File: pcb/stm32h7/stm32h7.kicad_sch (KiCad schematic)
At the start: 36 parts, among them SW2 SW_Push, SW3 SW_Push, U1 STM32H743VGTx, U11 TPS61169DCKR, U9 MT25QUxxxxxx1xW7, Y1 25MHz

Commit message: routing done
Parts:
- removed SW3: SW_Push, custom_comps:SW4_PTS815 SJM 250 SMTR LFS_CNK, symbol Switch:SW_Push
- added J6: Test Pads, custom_comps:2 Wire Pads, symbol Connector:Conn_01x02_Pin
- added SW1: SW_Push, custom_comps:vert_button_6mm, symbol Switch:SW_Push
- added SW3: SW_Push, SW4_PTS815 SJM 250 SMTR LFS_CNK, symbol PTS815_SJM_250_SMTR_LFS:PTS815_SJM_250_SMTR_LFS
- C14, C22: footprint (none) -> Capacitor_SMD:C_0402_1005Metric
- R2: footprint (none) -> Resistor_SMD:R_0402_1005Metric
- SW2: footprint custom_comps:SW4_PTS815 SJM 250 SMTR LFS_CNK -> SW4_PTS815 SJM 250 SMTR LFS_CNK; symbol Switch:SW_Push -> PTS815_SJM_250_SMTR_LFS:PTS815_SJM_250_SMTR_LFS
- U11: footprint DCK0005A_N -> custom_comps:DCK0005A_N
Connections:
- net +3V3: now also SW3.1, SW3.2
- net GND: now also SW2.3, SW2.4, Y1.2, SW1.2; no longer SW2.1, U1.24 (PA2), U1.32 (PC4), U1.33 (PC5), Y1.1
- net NRST: now also SW2.1
- net PH0: now also Y1.1; no longer Y1.2
- net at R1.1, U1.94 (BOOT0): now also SW3.3, SW3.4
- new net: J6.1 (Pin_1), U1.32 (PC4)
- new net: J6.2 (Pin_2), U1.24 (PA2)
- new net BTN: SW1.1, U1.33 (PC5)
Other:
- moved on the sheet: C5, C6, R1

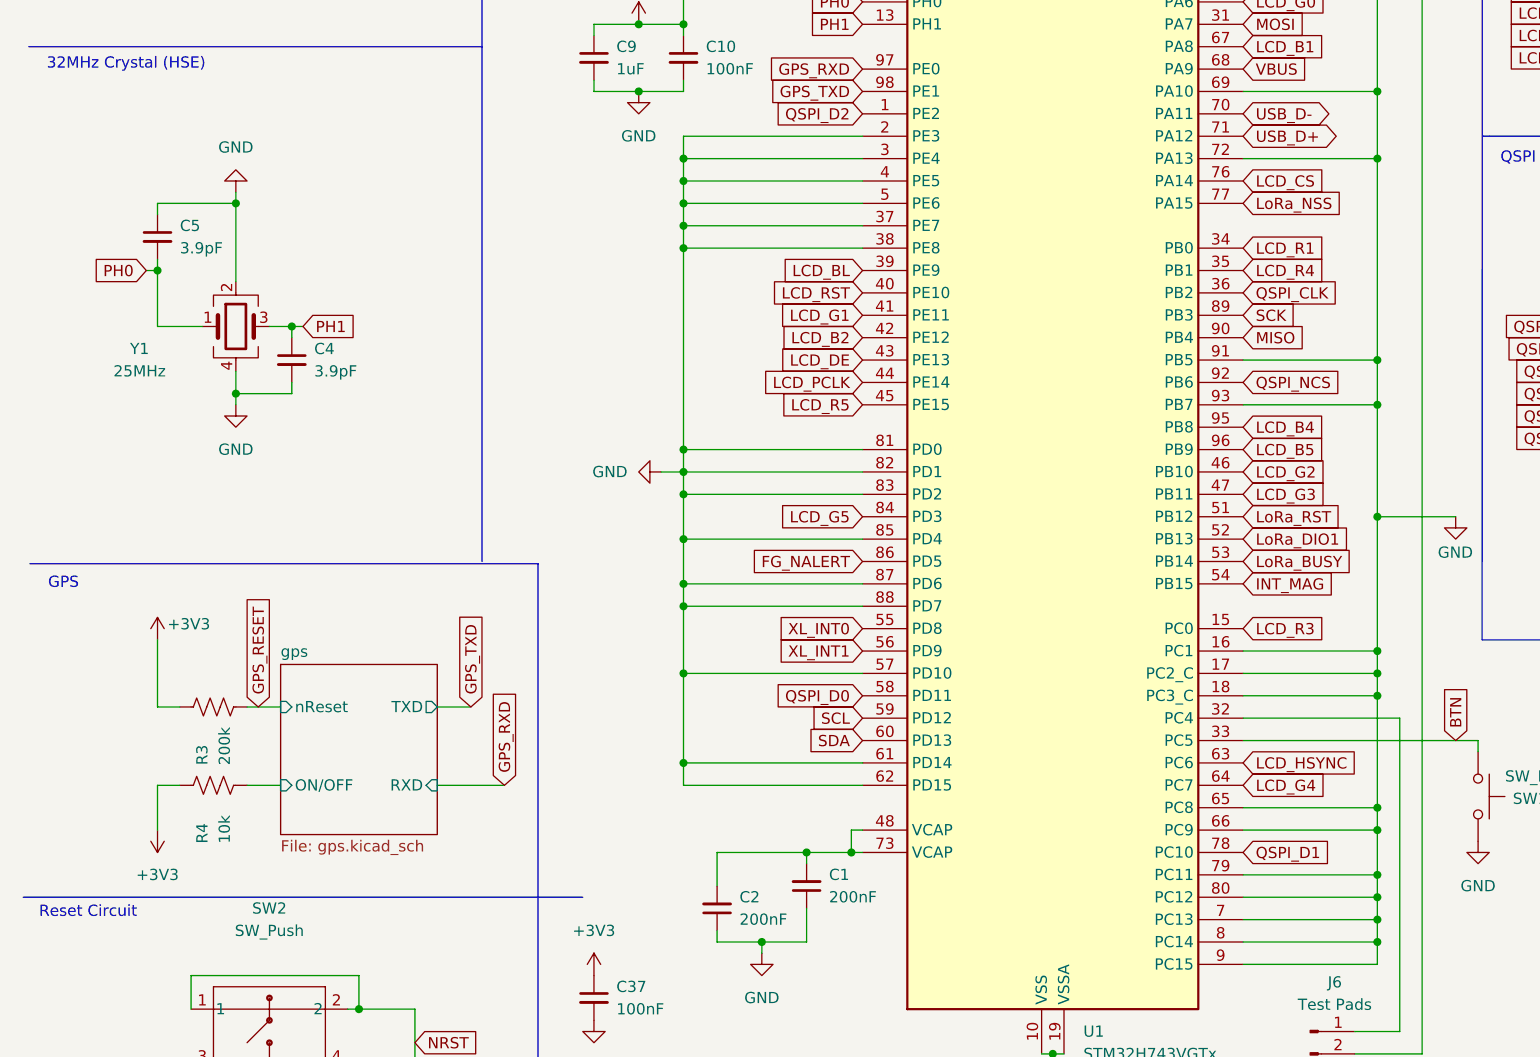
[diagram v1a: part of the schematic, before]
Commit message: fixed some footprints and added power switching mosfet for gps
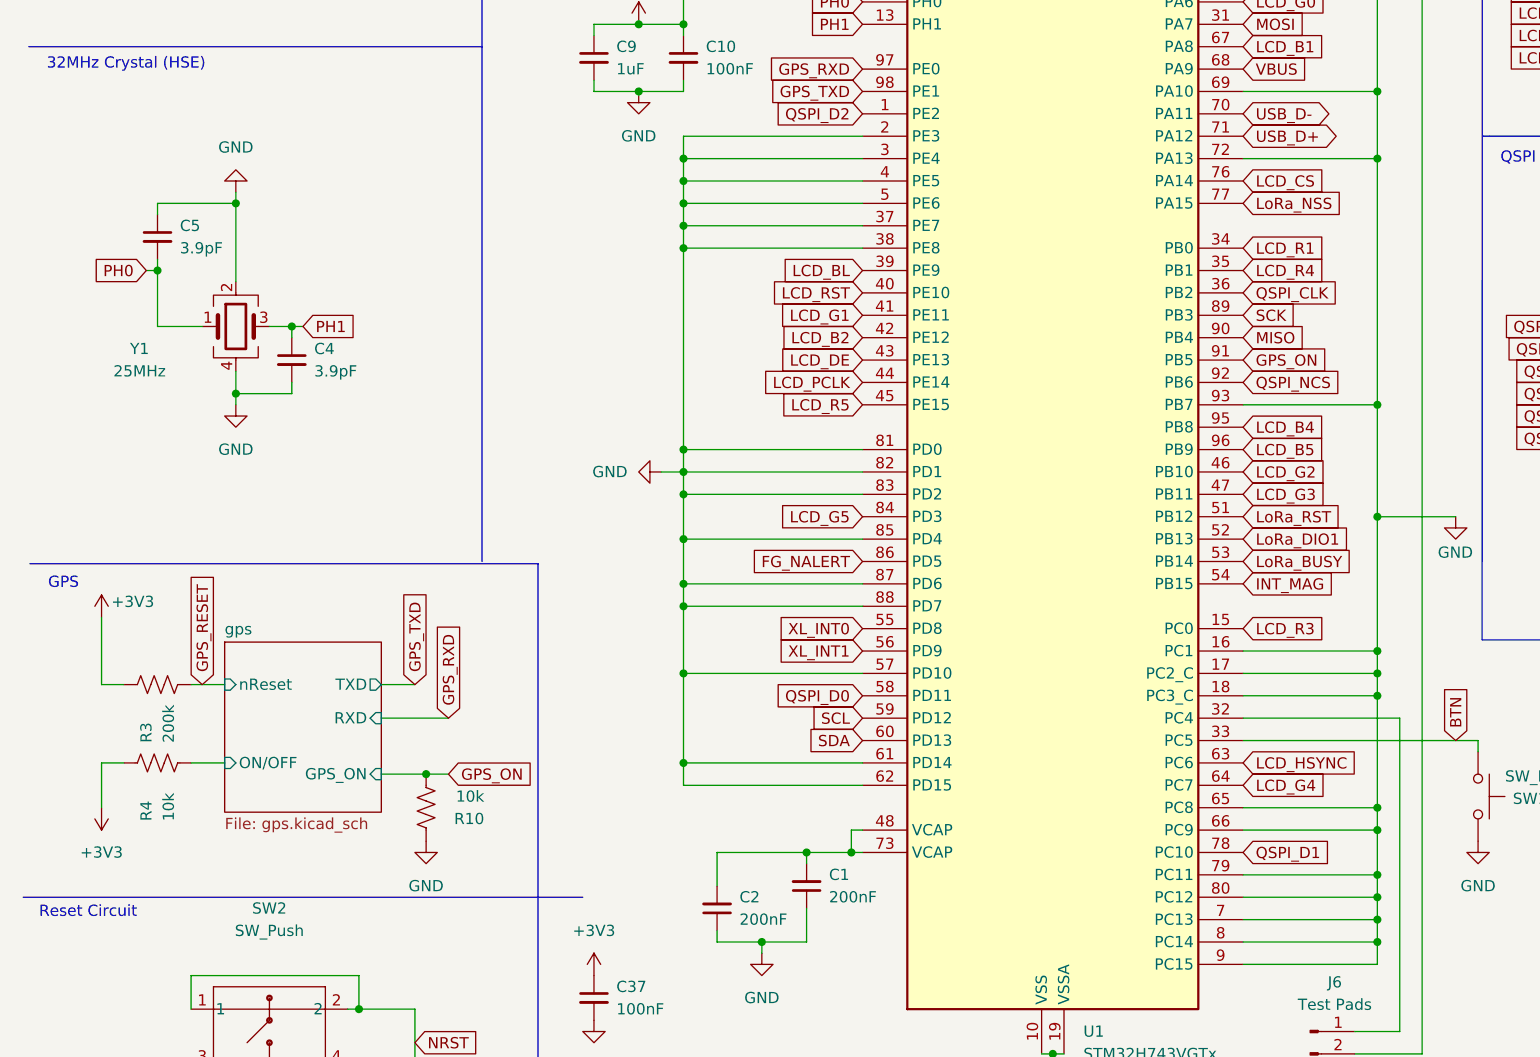
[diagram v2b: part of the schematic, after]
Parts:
- added R10: 10k, Resistor_SMD:R_0402_1005Metric, symbol Device:R_US
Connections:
- net GND: now also R10.1; no longer U1.91 (PB5)
- new net GPS_ON: R10.2, U1.91 (PB5)
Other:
- sheet gps ports: added GPS_ON; removed none
- moved on the sheet: R3, R4

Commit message: is it finally done or am i going insane
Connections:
- net GND: no longer U1.16 (PC1)
- new net PWR_ON: U1.16 (PC1)
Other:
- sheet Accel & Magnetometer ports: added none; removed CS_MAG, CS_XL
- moved on the sheet: SW1
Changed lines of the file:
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@@
 	)
 	(junction
-		(at 165.1 130.81)
-		(diameter 0)
-		(color 0 0 0 0)
-	)
-	(junction
 		(at 110.49 190.5)
 		(diameter 0)
@@
 	)
 	(junction
-		(at 165.1 163.83)
+		(at 177.8 140.97)
 		(diameter 0)
 		(color 0 0 0 0)
 	)
 	(junction
-		(at 228.6 31.75)
+		(at 165.1 163.83)
 		(diameter 0)
 		(color 0 0 0 0)
 	)
 	(junction
-		(at 87.63 185.42)
+		(at 228.6 31.75)
 		(diameter 0)
 		(color 0 0 0 0)
 	)
 	(junction
-		(at 165.1 115.57)
+		(at 87.63 185.42)
 		(diameter 0)
 		(color 0 0 0 0)
@@
 		(color 0 0 0 0)
 	)
+	(junction
+		(at 165.1 115.57)
+		(diameter 0)
+		(color 0 0 0 0)
+	)
 	(no_connect
 		(at 29.21 38.1)
@@
 	(wire
 		(pts
-			(xy 149.86 130.81) (xy 165.1 130.81)
-		)
-		(stroke
-			(width 0)
-			(type default)
-		)
-	)
-	(wire
-		(pts
 			(xy 104.14 34.29) (xy 104.14 38.1)
 		)
@@
 	(wire
 		(pts
-			(xy 165.1 130.81) (xy 165.1 133.35)
+			(xy 173.99 115.57) (xy 173.99 116.84)
 		)
 		(stroke
@@
 	(wire
 		(pts
+			(xy 165.1 115.57) (xy 165.1 133.35)
+		)
+		(stroke
+			(width 0)
+			(type default)
+		)
+	)
+	(wire
+		(pts
 			(xy 22.86 193.04) (xy 31.75 193.04)
 		)
@@
 	(wire
 		(pts
-			(xy 165.1 115.57) (xy 165.1 130.81)
-		)
-		(stroke
-			(width 0)
-			(type default)
-		)
-	)
-	(wire
-		(pts
 			(xy 144.78 190.5) (xy 156.21 190.5)
 		)
@@
 	(wire
 		(pts
+			(xy 177.8 140.97) (xy 177.8 138.43)
+		)
+		(stroke
+			(width 0)
+			(type default)
+		)
+	)
+	(wire
+		(pts
 			(xy 149.86 163.83) (xy 165.1 163.83)
 		)
@@
 	(wire
 		(pts
+			(xy 250.19 147.32) (xy 254 147.32)
+		)
+		(stroke
+			(width 0)
+			(type default)
+		)
+	)
+	(wire
+		(pts
 			(xy 95.25 163.83) (xy 95.25 165.1)
 		)
@@
 	(wire
 		(pts
+			(xy 149.86 140.97) (xy 177.8 140.97)
+		)
+		(stroke
+			(width 0)
+			(type default)
+		)
+	)
+	(wire
+		(pts
 			(xy 100.33 163.83) (xy 100.33 160.02)
 		)
@@
 	(wire
 		(pts
-			(xy 176.53 142.24) (xy 176.53 140.97)
+			(xy 177.8 144.78) (xy 177.8 140.97)
+		)
+		(stroke
+			(width 0)
+			(type default)
+		)
+	)
+	(wire
+		(pts
+			(xy 250.19 149.86) (xy 254 149.86)
 		)
 		(stroke
@@
 	(wire
 		(pts
-			(xy 149.86 140.97) (xy 176.53 140.97)
-		)
-		(stroke
-			(width 0)
-			(type default)
-		)
-	)
-	(wire
-		(pts
 			(xy 30.48 177.8) (xy 30.48 181.61)
 		)
@@
 	(global_label "SCL"
 		(shape input)
-		(at 250.19 146.05 0)
+		(at 254 147.32 0)
 		(fields_autoplaced yes)
 		(effects
@@
 		)
 		(property "Intersheetrefs" "${INTERSHEET_REFS}"
-			(at 256.6828 146.05 0)
+			(at 260.4928 147.32 0)
 			(effects
 				(font
@@
 		)
 	)
+	(global_label "PWR_ON"
+		(shape input)
+		(at 149.86 130.81 0)
+		(fields_autoplaced yes)
+		(effects
+			(font
+				(size 1.27 1.27)
+			)
+			(justify left)
+		)
+		(property "Intersheetrefs" "${INTERSHEET_REFS}"
+			(at 160.4652 130.81 0)
+			(effects
+				(font
+					(size 1.27 1.27)
+				)
+				(justify left)
+				(hide yes)
+			)
+		)
+	)
 	(global_label "LCD_CS"
 		(shape input)
@@
 	(global_label "SDA"
 		(shape input)
-		(at 250.19 143.51 0)
+		(at 254 149.86 0)
 		(fields_autoplaced yes)
 		(effects
@@
 		)
 		(property "Intersheetrefs" "${INTERSHEET_REFS}"
-			(at 256.7433 143.51 0)
+			(at 260.5533 149.86 0)
 			(effects
 				(font
@@
 	(global_label "BTN"
 		(shape input)
-		(at 173.99 140.97 90)
+		(at 177.8 138.43 90)
 		(fields_autoplaced yes)
 		(effects
@@
 		)
 		(property "Intersheetrefs" "${INTERSHEET_REFS}"
-			(at 173.99 134.4167 90)
+			(at 177.8 131.8767 90)
 			(effects
 				(font
@@
 	(symbol
 		(lib_id "Switch:SW_Push")
-		(at 176.53 147.32 270)
+		(at 177.8 149.86 270)
 		(unit 1)
 		(exclude_from_sim no)
@@
 		(dnp no)
 		(property "Reference" "SW1"
-			(at 184.404 147.574 90)
+			(at 185.674 150.114 90)
 			(effects
 				(font
@@
 		)
 		(property "Value" "SW_Push"
-			(at 187.452 145.034 90)
+			(at 188.722 147.574 90)
 			(effects
 				(font
@@
 		)
 		(property "Footprint" "custom_comps:vert_button_6mm"
-			(at 181.61 147.32 0)
+			(at 182.88 149.86 0)
 			(effects
 				(font
@@
 		)
 		(property "Datasheet" "~"
-			(at 181.61 147.32 0)
+			(at 182.88 149.86 0)
 			(effects
 				(font
@@
 		)
 		(property "Description" "Push button switch, generic, two pins"
-			(at 176.53 147.32 0)
+			(at 177.8 149.86 0)
 			(effects
 				(font
@@
 	(symbol
 		(lib_id "power:GND")
-		(at 176.53 152.4 0)
+		(at 177.8 154.94 0)
 		(unit 1)
 		(exclude_from_sim no)
@@
 		(fields_autoplaced yes)
 		(property "Reference" "#PWR082"
-			(at 176.53 158.75 0)
+			(at 177.8 161.29 0)
 			(effects
 				(font
@@
 		)
 		(property "Value" "GND"
-			(at 176.53 157.48 0)
+			(at 177.8 160.02 0)
 			(effects
 				(font
@@
 		)
 		(property "Footprint" ""
-			(at 176.53 152.4 0)
+			(at 177.8 154.94 0)
 			(effects
 				(font
@@
 		)
 		(property "Datasheet" ""
-			(at 176.53 152.4 0)
+			(at 177.8 154.94 0)
 			(effects
 				(font
@@
 		)
 		(property "Description" "Power symbol creates a global label with name \"GND\" , ground"
-			(at 176.53 152.4 0)
+			(at 177.8 154.94 0)
 			(effects
 				(font
@@
 	(symbol
 		(lib_id "power:GND")
-		(at 173.99 115.57 0)
+		(at 173.99 116.84 0)
 		(unit 1)
 		(exclude_from_sim no)
@@
 		(dnp no)
 		(property "Reference" "#PWR077"
-			(at 173.99 121.92 0)
+			(at 173.99 123.19 0)
 			(effects
 				(font
@@
 		)
 		(property "Value" "GND"
-			(at 171.958 119.634 0)
+			(at 171.958 120.904 0)
 			(effects
 				(font
@@
 		)
 		(property "Footprint" ""
-			(at 173.99 115.57 0)
+			(at 173.99 116.84 0)
 			(effects
 				(font
@@
 		)
 		(property "Datasheet" ""
-			(at 173.99 115.57 0)
+			(at 173.99 116.84 0)
 			(effects
 				(font
@@
 		)
 		(property "Description" "Power symbol creates a global label with name \"GND\" , ground"
-			(at 173.99 115.57 0)
+			(at 173.99 116.84 0)
 			(effects
 				(font
@@
 		)
 		(pin "SDA" bidirectional
-			(at 250.19 146.05 0)
+			(at 250.19 149.86 0)
 			(effects
 				(font
@@
 		)
 		(pin "SCL" bidirectional
-			(at 250.19 143.51 0)
+			(at 250.19 147.32 0)
 			(effects
 				(font
@@
 			)
 		)
-		(pin "CS_XL" input
-			(at 250.19 148.59 0)
-			(effects
-				(font
-					(size 1.27 1.27)
-				)
-				(justify right)
-			)
-		)
-		(pin "CS_MAG" input
-			(at 250.19 151.13 0)
-			(effects
-				(font
-					(size 1.27 1.27)
-				)
-				(justify right)
-			)
-		)

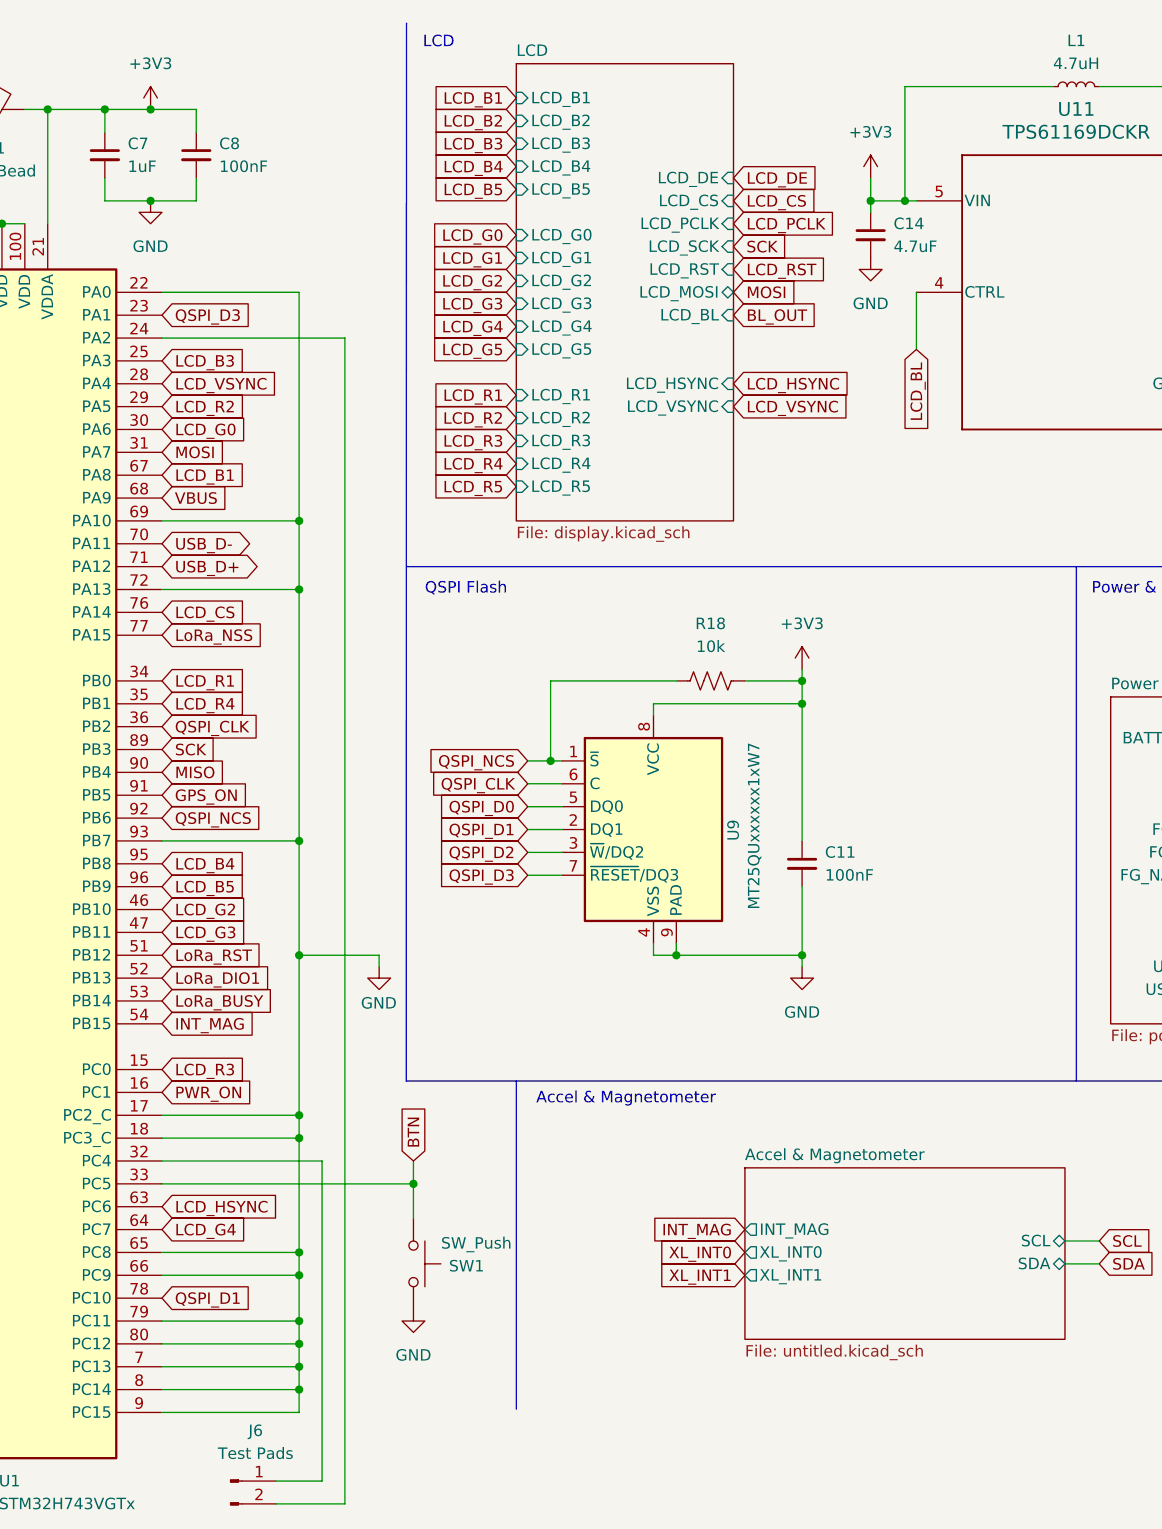
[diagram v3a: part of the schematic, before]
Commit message: using EN on the LDO for power switch now
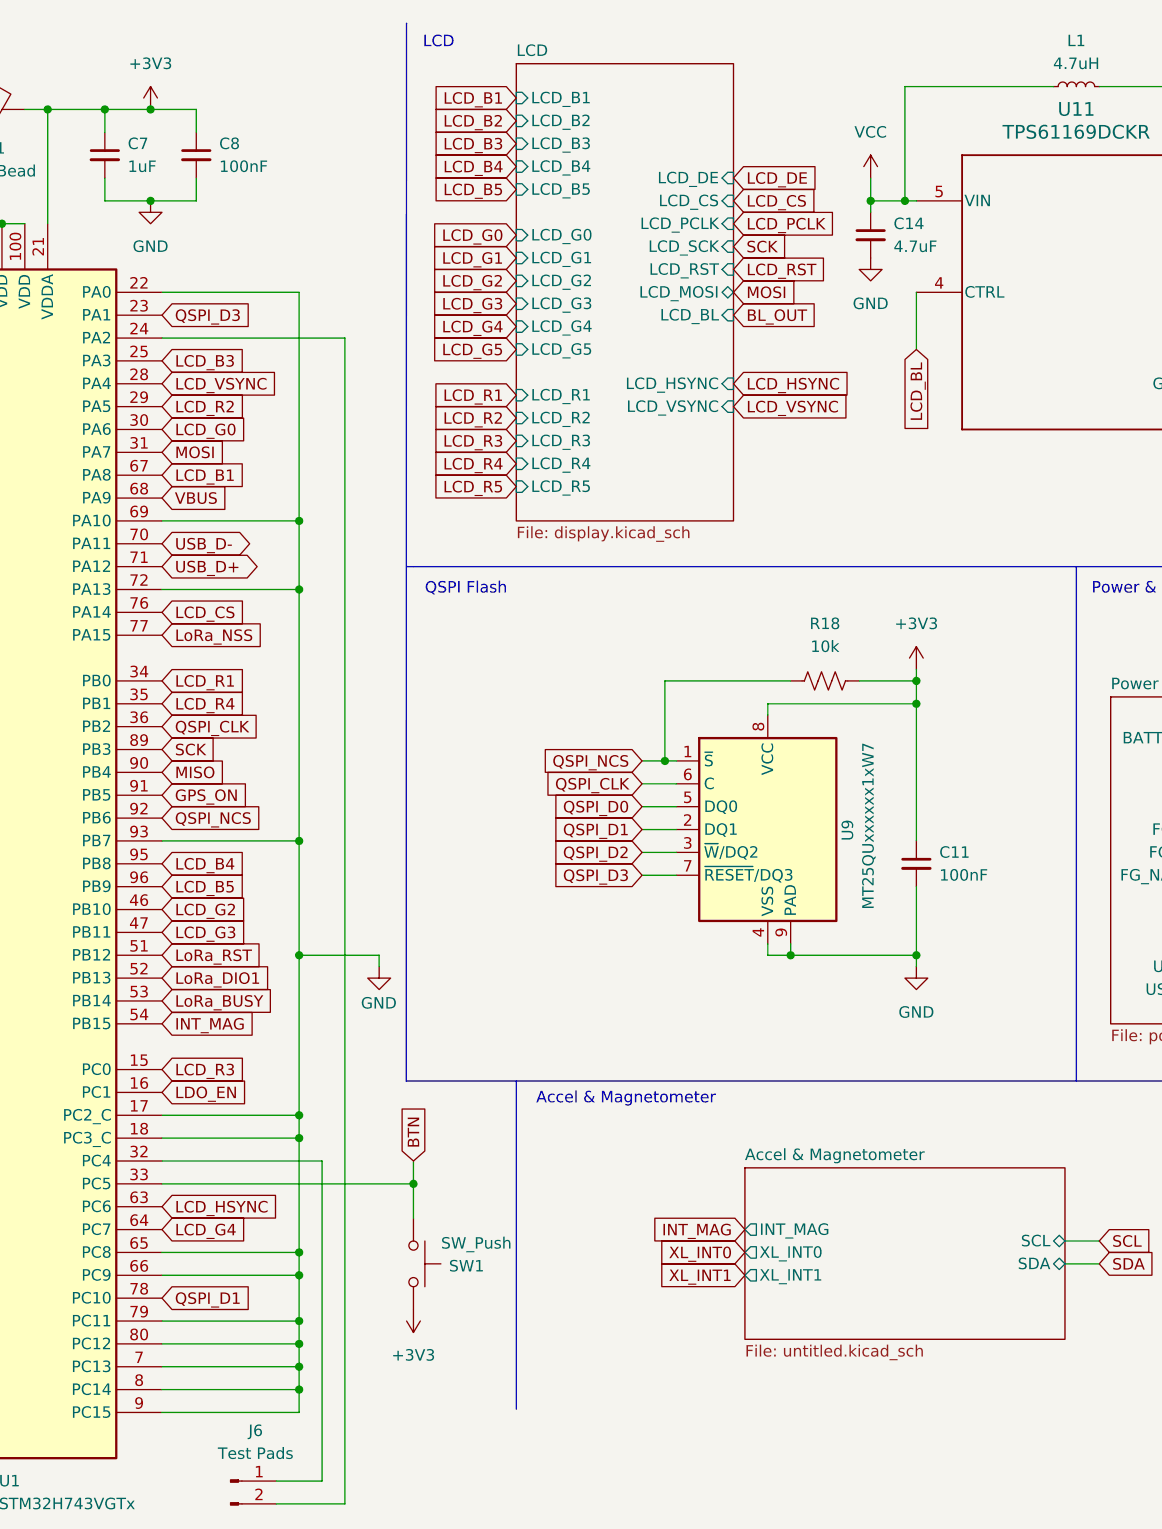
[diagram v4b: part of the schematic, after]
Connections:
- net +3V3: now also SW1.2; no longer C14.1, L1.1, U11.5 (VIN)
- net GND: no longer SW1.2
- net PWR_ON renamed LDO_EN
- new net VCC: C14.1, L1.1, U11.5 (VIN)
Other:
- moved on the sheet: C11, R18, U9

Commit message: fixed some wiring
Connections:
- net GND: now also R2.1; no longer R2.2
- net BL_OUT renamed BL_ANODE
- net BL_ANODE: no longer R2.1, U11.3 (FB)
- new net BL_CATHODE: R2.2, U11.3 (FB)
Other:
- sheet LCD ports: added LCD_BL_ANODE, LCD_BL_CATHODE; removed LCD_BL
